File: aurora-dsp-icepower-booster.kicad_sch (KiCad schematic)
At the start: 264 parts, among them J1 24V DC, J10 XLR3_OUT, J11 XLR3_OUT, J12 XLR3_OUT, J13 XLR3_OUT, J14 XLR3_OUT, J2 REMOTE 3.5mm, J3 XLR_IN_1, J4 XLR_IN_2, J5 XLR_IN_3, J6 XLR_IN_4, J7 XLR_IN_5, J8 XLR_IN_6, J9 XLR3_OUT, Q1 BSS138, Q2 BSS138, Q3 BSS138, Q4 BSS138, Q5 BSS138, Q6 BSS138, Q7 BSS138, SW1 ALWAYS/REMOTE, SW2 Gain CH1, SW3 Gain CH2, SW4 Gain CH3, SW5 Gain CH4, SW6 Gain CH5, SW7 Gain CH6, U1 TEL5-2422, U10 LM4562, U11 LM4562, U12 LM4562, U13 LM4562, U14 ADP7118ARDZ-11, U15 ADP7182AUJZ-11, U2 LM4562, U3 LM4562, U4 LM4562, U5 LM4562, U6 LM4562, U7 LM4562, U8 LM4562, U9 LM4562

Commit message: fix: ESD Dioden D8/D9/D11-D15/D17-D21/D23/D24 korrekt verdrahtet
- 18 fehlerhafte GND-Wires gelöscht (D_upper.A und D_lower.A lagen auf same GND-Wire)
- 6 neue Wires (285,y_top)→(285,y_A_upper) für CHn_HOT_RAW → D_upper.A
- 6 neue Labels CH{1-6}_OUT_COLD bei D_lower.A-Pin für Anode-Verbindung
- Alle 24 ESD-Dioden jetzt korrekt: A=Signal, K=GND
- ERC: 0 Errors (war 1 Error vor Fix), 1059 Warnings (+8 endpoint_off_grid kosmetisch)
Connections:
- net CH1_HOT_RAW: now also D8.2 (A)
- net CH1_OUT_COLD: now also D9.2 (A)
- net CH2_HOT_RAW: now also D11.2 (A)
- net CH2_OUT_COLD: now also D12.2 (A)
- net CH3_HOT_RAW: now also D14.2 (A)
- net CH3_OUT_COLD: now also D15.2 (A)
- net CH4_HOT_RAW: now also D17.2 (A)
- net CH4_OUT_COLD: now also D18.2 (A)
- net CH5_HOT_RAW: now also D20.2 (A)
- net CH5_OUT_COLD: now also D21.2 (A)
- net CH6_HOT_RAW: now also D23.2 (A)
- net CH6_OUT_COLD: now also D24.2 (A)
- net GND: no longer D11.2 (A), D12.2 (A), D14.2 (A), D15.2 (A), D17.2 (A), D18.2 (A), D20.2 (A), D21.2 (A), D23.2 (A), D24.2 (A), D8.2 (A), D9.2 (A)
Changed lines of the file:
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@@
   (wire (pts (xy 127.62 530) (xy 125.08 530)) (stroke (width 0) (type default)))
   (wire (pts (xy 30 117.62) (xy 30 120)) (stroke (width 0) (type default)))
-  (wire (pts (xy 285 185.19) (xy 285 186.19)) (stroke (width 0) (type default)))
   (wire (pts (xy 195 288.81) (xy 195 291.35)) (stroke (width 0) (type default)))
   (wire (pts (xy 87.38 552.54) (xy 89.92 552.54)) (stroke (width 0) (type default)))
@@
   (wire (pts (xy 276.86 197.62) (xy 271.78 197.62)) (stroke (width 0) (type default)))
   (wire (pts (xy 87.38 550) (xy 89.92 550)) (stroke (width 0) (type default)))
-  (wire (pts (xy 285 265.19) (xy 285 266.19)) (stroke (width 0) (type default)))
   (wire (pts (xy 37.62 270) (xy 42 270)) (stroke (width 0) (type default)))
   (wire (pts (xy 162.38 427.46) (xy 177.62 430)) (stroke (width 0) (type default)))
@@
   (wire (pts (xy 65 356.19) (xy 65 353.65)) (stroke (width 0) (type default)))
   (wire (pts (xy 105 323.81) (xy 105 326.35)) (stroke (width 0) (type default)))
-  (wire (pts (xy 285 105.19) (xy 285 106.19)) (stroke (width 0) (type default)))
   (wire (pts (xy 165 178.81) (xy 165 181.35)) (stroke (width 0) (type default)))
   (wire (pts (xy 102.62 552.54) (xy 105 556.19)) (stroke (width 0) (type default)))
   (wire (pts (xy 42 85) (xy 42 82.46)) (stroke (width 0) (type default)))
   (wire (pts (xy 280 425) (xy 285 425)) (stroke (width 0) (type default)))
-  (wire (pts (xy 285 425.19) (xy 285 426.19)) (stroke (width 0) (type default)))
   (wire (pts (xy 302 265) (xy 302 266.19)) (stroke (width 0) (type default)))
   (wire (pts (xy 251.46 197.62) (xy 246.38 197.62)) (stroke (width 0) (type default)))
@@
   (wire (pts (xy 285 113.81) (xy 285 115)) (stroke (width 0) (type default)))
     (wire (pts (xy 285 115) (xy 285 117)) (stroke (width 0) (type default)))
-  (wire (pts (xy 285 505.19) (xy 285 506.19)) (stroke (width 0) (type default)))
   (wire (pts (xy 202.38 192.54) (xy 204.92 192.54)) (stroke (width 0) (type default)))
   (wire (pts (xy 85 100.81) (xy 85 103.35)) (stroke (width 0) (type default)))
@@
   (wire (pts (xy 265 512.81) (xy 265 514.19)) (stroke (width 0) (type default)))
   (wire (pts (xy 265 104) (xy 265 105.19)) (stroke (width 0) (type default)))
-  (wire (pts (xy 285 345.19) (xy 285 346.19)) (stroke (width 0) (type default)))
   (wire (pts (xy 125 28.81) (xy 125 31.35)) (stroke (width 0) (type default)))
   (wire (pts (xy 175 171.19) (xy 175 168.65)) (stroke (width 0) (type default)))
@@
   (wire (pts (xy 251.46 502.38) (xy 246.38 502.38)) (stroke (width 0) (type default)))
   (wire (pts (xy 309.62 505) (xy 315 505)) (stroke (width 0) (type default)))
-  (wire (pts (xy 285.0 105.19) (xy 285.0 106.19)) (stroke (width 0) (type default)))
-  (wire (pts (xy 285.0 106.19) (xy 285.0 112.81)) (stroke (width 0) (type default)))
   (wire (pts (xy 285.0 112.81) (xy 285.0 113.81)) (stroke (width 0) (type default)))
-  (wire (pts (xy 285.0 185.19) (xy 285.0 186.19)) (stroke (width 0) (type default)))
-  (wire (pts (xy 285.0 186.19) (xy 285.0 192.81)) (stroke (width 0) (type default)))
   (wire (pts (xy 285.0 192.81) (xy 285.0 193.81)) (stroke (width 0) (type default)))
-  (wire (pts (xy 285.0 265.19) (xy 285.0 266.19)) (stroke (width 0) (type default)))
-  (wire (pts (xy 285.0 266.19) (xy 285.0 272.81)) (stroke (width 0) (type default)))
   (wire (pts (xy 285.0 272.81) (xy 285.0 273.81)) (stroke (width 0) (type default)))
-  (wire (pts (xy 285.0 345.19) (xy 285.0 346.19)) (stroke (width 0) (type default)))
-  (wire (pts (xy 285.0 346.19) (xy 285.0 352.81)) (stroke (width 0) (type default)))
   (wire (pts (xy 285.0 352.81) (xy 285.0 353.81)) (stroke (width 0) (type default)))
-  (wire (pts (xy 285.0 425.19) (xy 285.0 426.19)) (stroke (width 0) (type default)))
-  (wire (pts (xy 285.0 426.19) (xy 285.0 432.81)) (stroke (width 0) (type default)))
   (wire (pts (xy 285.0 432.81) (xy 285.0 433.81)) (stroke (width 0) (type default)))
-  (wire (pts (xy 285.0 505.19) (xy 285.0 506.19)) (stroke (width 0) (type default)))
-  (wire (pts (xy 285.0 506.19) (xy 285.0 512.81)) (stroke (width 0) (type default)))
   (wire (pts (xy 285.0 512.81) (xy 285.0 513.81)) (stroke (width 0) (type default)))
   (label "CH6_GAIN_FB" (at 195 521.19 0) (effects (font (size 1.27 1.27)) (justify left bottom)))
@@
       (project "aurora-dsp-icepower-booster"
   (path "/09fde901-d8c0-4b5a-a63a-824cb2cd0bb6" (reference "#PWR0152") (unit 1)))))
-  )
+    (wire (pts (xy 285 105) (xy 285 105.19)) (stroke (width 0) (type default)))
+  (label "CH1_OUT_COLD" (at 285 106.19 180) (effects (font (size 1.27 1.27)) (justify left bottom)))
+  (wire (pts (xy 285 185) (xy 285 185.19)) (stroke (width 0) (type default)))
+  (label "CH2_OUT_COLD" (at 285 186.19 180) (effects (font (size 1.27 1.27)) (justify left bottom)))
+  (wire (pts (xy 285 265) (xy 285 265.19)) (stroke (width 0) (type default)))
+  (label "CH3_OUT_COLD" (at 285 266.19 180) (effects (font (size 1.27 1.27)) (justify left bottom)))
+  (wire (pts (xy 285 345) (xy 285 345.19)) (stroke (width 0) (type default)))
+  (label "CH4_OUT_COLD" (at 285 346.19 180) (effects (font (size 1.27 1.27)) (justify left bottom)))
+  (wire (pts (xy 285 425) (xy 285 425.19)) (stroke (width 0) (type default)))
+  (label "CH5_OUT_COLD" (at 285 426.19 180) (effects (font (size 1.27 1.27)) (justify left bottom)))
+  (wire (pts (xy 285 505) (xy 285 505.19)) (stroke (width 0) (type default)))
+  (label "CH6_OUT_COLD" (at 285 506.19 180) (effects (font (size 1.27 1.27)) (justify left bottom)))
+)

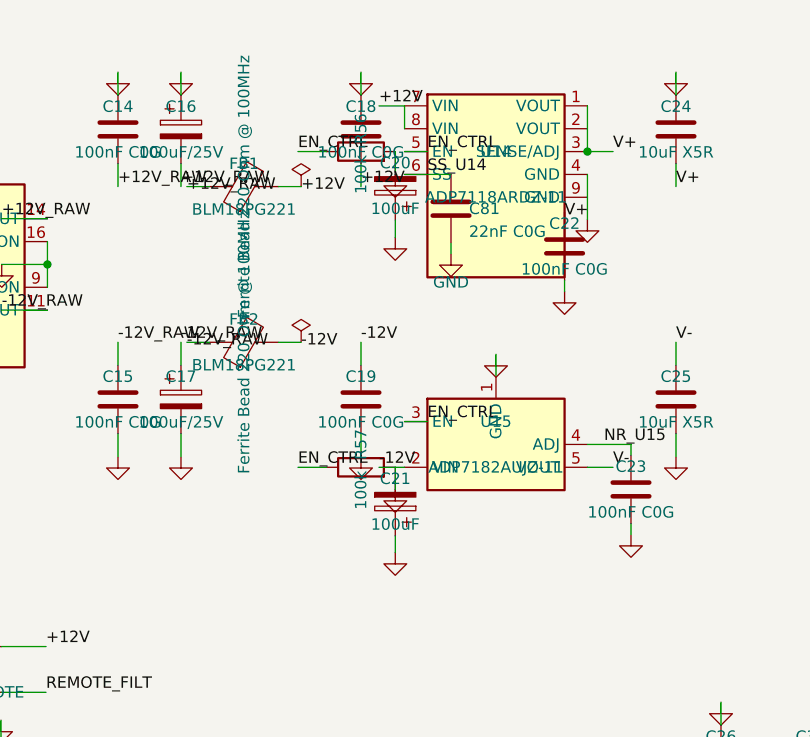
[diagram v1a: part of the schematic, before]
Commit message: Fix C20/C21: LDO output bulk caps now correctly connected to V+/V- rails
- C20 (100uF): Pin1=GND, Pin2=V+ (LDO positive output bulk capacitor)
- C21 (100uF): Pin1=V-, Pin2=GND (LDO negative output bulk capacitor)

Previously both caps had both pins connected to GND, providing zero filtering.
Removed 2x erroneous GND power symbols and wires, added V+/V- net labels.

ERC: 0 errors, 1055 warnings (all pre-existing endpoint_off_grid)
Netlist validation: all signal chains pass, C20/C21 now on correct rails.
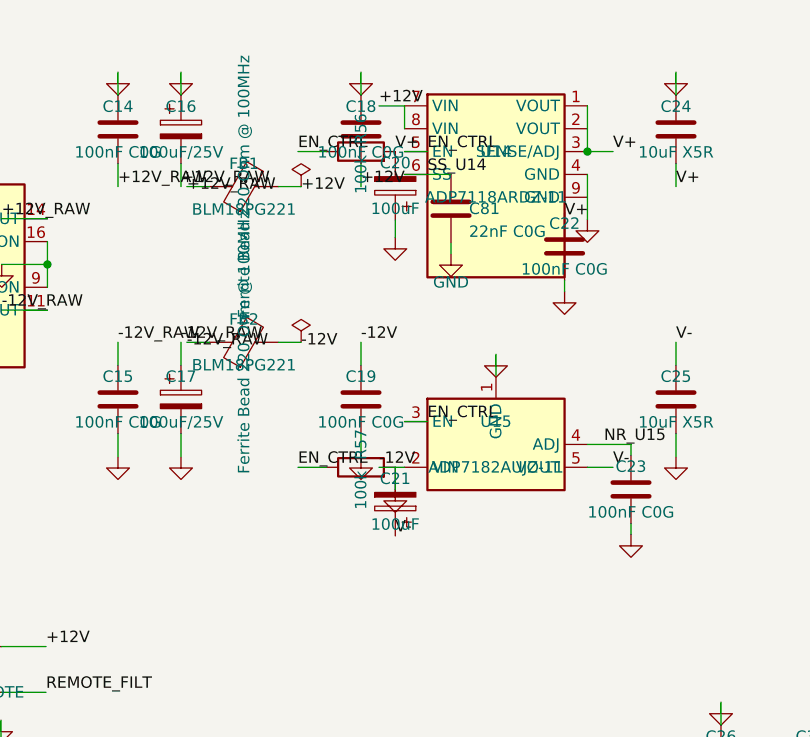
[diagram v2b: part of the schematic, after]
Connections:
- net GND: no longer C20.2, C21.1, R56.2
- net V+: now also C20.2, R56.2
- net V-: now also C21.1
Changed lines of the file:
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@@
   (wire (pts (xy 22.38 430) (xy 24.92 430)) (stroke (width 0) (type default)))
   (wire (pts (xy 102.62 387.46) (xy 105 376.19)) (stroke (width 0) (type default)))
-  (wire (pts (xy 128.81 27.46) (xy 128.81 30)) (stroke (width 0) (type default)))
   (wire (pts (xy 120 523.81) (xy 127.62 530)) (stroke (width 0) (type default)))
   (wire (pts (xy 105 473.81) (xy 105 475)) (stroke (width 0) (type default)))
@@
   (wire (pts (xy 190 93.81) (xy 190 96.35)) (stroke (width 0) (type default)))
   (wire (pts (xy 105 233.81) (xy 105 235)) (stroke (width 0) (type default)))
-  (wire (pts (xy 128.81 70.16) (xy 128.81 72)) (stroke (width 0) (type default)))
   (wire (pts (xy 98.0 21.19) (xy 98.0 18.65)) (stroke (width 0) (type default)) (uuid "rejoin-98-vert"))
   (wire (pts (xy 98 58.81) (xy 98 61.35)) (stroke (width 0) (type default)))
@@
       (project "aurora-dsp-icepower-booster"
   (path "/09fde901-d8c0-4b5a-a63a-824cb2cd0bb6" (reference "#PWR030") (unit 1)))))
-  (symbol (lib_id "power:GND") (at 128.81 30 0) (unit 1) (exclude_from_sim no) (in_bom yes) (on_board yes) (dnp no)
-    (property "Reference" "#PWR031" (at 128.81 30 0) (effects (font (size 1.27 1.27)) (hide yes)))
-    (property "Value" "GND" (at 128.81 30 0) (effects (font (size 1.27 1.27)) (hide yes)))
-    (property "Footprint" "" (at 128.81 30 0) (effects (font (size 1.27 1.27)) (hide yes)))
-    (property "Datasheet" "" (at 128.81 30 0) (effects (font (size 1.27 1.27)) (hide yes)))
-    (pin "1")
-    (instances
-      (project "aurora-dsp-icepower-booster"
-  (path "/09fde901-d8c0-4b5a-a63a-824cb2cd0bb6" (reference "#PWR031") (unit 1)))))
   (symbol (lib_id "power:GND") (at 98 61.35 0) (unit 1) (exclude_from_sim no) (in_bom yes) (on_board yes) (dnp no)
     (property "Reference" "#PWR032" (at 98 61.35 0) (effects (font (size 1.27 1.27)) (hide yes)))
@@
   (label "EN_CTRL" (at 132.38 57.46 0) (effects (font (size 1.27 1.27)) (justify left bottom)))
   (label "CH1_RX_OUT" (at 92 110 0) (effects (font (size 1.27 1.27)) (justify left bottom)))
-  (symbol (lib_id "power:GND") (at 128.81 72 0) (unit 1) (exclude_from_sim no) (in_bom yes) (on_board yes) (dnp no)
-    (property "Reference" "#PWR038" (at 128.81 72 0) (effects (font (size 1.27 1.27)) (hide yes)))
-    (property "Value" "GND" (at 128.81 72 0) (effects (font (size 1.27 1.27)) (hide yes)))
-    (property "Footprint" "" (at 128.81 72 0) (effects (font (size 1.27 1.27)) (hide yes)))
-    (property "Datasheet" "" (at 128.81 72 0) (effects (font (size 1.27 1.27)) (hide yes)))
-    (pin "1")
-    (instances
-      (project "aurora-dsp-icepower-booster"
-  (path "/09fde901-d8c0-4b5a-a63a-824cb2cd0bb6" (reference "#PWR038") (unit 1)))))
   (label "V+" (at 271.78 102.38 0) (effects (font (size 1.27 1.27)) (justify left bottom)))
   (label "V+" (at 165 421.35 0) (effects (font (size 1.27 1.27)) (justify left bottom)))
@@
   (label "CH5_OUT_COLD" (at 285 426.19 180) (effects (font (size 1.27 1.27)) (justify left bottom)))
   (wire (pts (xy 285 505) (xy 285 505.19)) (stroke (width 0) (type default)))
-  (label "CH6_OUT_COLD" (at 285 506.19 180) (effects (font (size 1.27 1.27)) (justify left bottom)))
+  (label "CH6_OUT_COLD" (at 285 506.19 180) (effects (font (size 1.27 1.27)) (justify left bottom)))(label "V+" (at 128.81 27.46 0) (effects (font (size 1.27 1.27)) (justify left bottom)))(label "V-" (at 128.81 70.16 0) (effects (font (size 1.27 1.27)) (justify left bottom)))
 )
